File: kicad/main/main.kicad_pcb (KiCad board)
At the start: 2 copper layers, 41 x 41 mm, 11 parts, among them J1 Conn_01x14, J2 Conn_01x14_Socket, J3 Conn_01x04, J4 Conn_01x03_Socket, J5 Conn_01x06, J7 Conn_01x07, J8 Conn_01x09

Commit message: modified:   kicad/main/main.kicad_pcb
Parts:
- added D1: LED, LED_THT:LED_D3.0mm_FlatTop, F.Cu at (135.8, 72.0)
- added R1: R, Resistor_THT:R_Axial_DIN0204_L3.6mm_D1.6mm_P5.08mm_Horizontal, F.Cu at (134.0, 81.2)
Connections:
- J1 pad 11: unconnected-(J1-Pin_11-Pad11) -> /LED
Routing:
- net Net-(D1-A): track 0.00 -> 19.9 mm
- net /GND: track 45.7 -> 61.8 mm
- net /LED: track 0.00 -> 6.01 mm
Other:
- board text added: ">LED"
- board text added: "CS"
- board text added: "LED>"
- board text added: "MISO"
- board text added: "MOSI"
- board text removed: "GND"

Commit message: modified:   kicad/main/main.kicad_pcb
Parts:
- added G***: LOGO, Logo:logo, F.Cu at (145.9, 83.9)

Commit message: modified:   kicad/main/main.kicad_pcb
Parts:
- added J6: Conn_01x08, Connector_PinSocket_2.00mm:PinSocket_1x08_P2.00mm_Vertical, F.Cu at (137.8, 107.5)
- moved R1 1.04 mm to (132.9, 81.2)
- moved G*** 0.69 mm to (145.2, 83.8)
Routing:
- net /MOSI: track 0.00 -> 38.1 mm
- net /MISO: track 0.00 -> 36.3 mm
- net /CS: track 0.00 -> 35.6 mm
- net /SCL1: track 0.00 -> 21.4 mm
- net /SDA1: track 0.00 -> 20.8 mm
- net /SCK: track 0.00 -> 20.4 mm
- net /3V3: track 37.2 -> 42.1 mm
- net /GND: track 61.8 -> 60.1 mm
- net Net-(D1-A): track 19.9 -> 18.8 mm
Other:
- board size 41 x 41 mm -> 41 x 44.5 mm
- board text added: "CL1"
- board text added: "DA1"
- board text added: "SCK"
- board text added: "SI"
- board text added: "SO"

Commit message: modified:   kicad/main/main.kicad_pcb
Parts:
- removed ? (x2): , 
- removed J3: Conn_01x04, Connector_PinHeader_2.00mm:PinHeader_1x04_P2.00mm_Vertical
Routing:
- net /5V: track 24.2 -> 9.60 mm
- net /RX5: track 11.5 -> 0.00 mm
- net /TX5: track 11.2 -> 0.00 mm
- net /GND: track 60.1 -> 57.6 mm

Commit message: modified:   kicad/main/main.kicad_pcb
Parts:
- 220Ω: renamed from R1; footprint Resistor_THT:R_Axial_DIN0204_L3.6mm_D1.6mm_P5.08mm_Horizontal -> Resistor_THT:R_Axial_DIN0204_L3.6mm_D1.6mm_P7.62mm_Horizontal
- moved 220Ω 0.77 mm to (132.8, 80.5), turned to -90 degrees
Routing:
- net /LED: track 5.58 -> 13.5 mm

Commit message: modified:   kicad/main/main.kicad_pcb
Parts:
- added ?: , , F.Cu at (145.2, 104.8)
- added ?: , , F.Cu at (127.8, 86.2)
- moved J6 0.50 mm to (137.8, 108.0)
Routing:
- net /SDA1: track 20.8 -> 21.3 mm
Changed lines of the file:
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@@
 	(footprint "Connector_PinSocket_2.00mm:PinSocket_1x08_P2.00mm_Vertical"
 		(layer "F.Cu")
-		(at 137.75 107.5 90)
+		(at 137.75 108 90)
 		(descr "Through hole straight socket strip, 1x08, 2.00mm pitch, single row (from Kicad 4.0.7), script generated")
 		(tags "Through hole socket strip THT 1x08 2.00mm single row")
@@
 		)
 	)
+	(footprint ""
+		(layer "F.Cu")
+		(at 145.25 104.75)
+		(property "Reference" ""
+			(at 0 0 0)
+			(layer "F.SilkS")
+			(effects
+				(font
+					(size 1.27 1.27)
+					(thickness 0.15)
+				)
+			)
+		)
+		(property "Value" ""
+			(at 0 0 0)
+			(layer "F.Fab")
+			(effects
+				(font
+					(size 1.27 1.27)
+					(thickness 0.15)
+				)
+			)
+		)
+		(property "Datasheet" ""
+			(at 0 0 0)
+			(layer "F.Fab")
+			(hide yes)
+			(effects
+				(font
+					(size 1.27 1.27)
+					(thickness 0.15)
+				)
+			)
+		)
+		(property "Description" ""
+			(at 0 0 0)
+			(layer "F.Fab")
+			(hide yes)
+			(effects
+				(font
+					(size 1.27 1.27)
+					(thickness 0.15)
+				)
+			)
+		)
+		(pad "" np_thru_hole circle
+			(at 0.132999 -0.264 225)
+			(size 2.5 2.5)
+			(drill 2.5)
+			(layers "*.Cu" "*.Mask")
+		)
+		(embedded_fonts no)
+	)
 	(footprint "Connector_PinHeader_2.54mm:PinHeader_1x03_P2.54mm_Vertical"
 		(layer "F.Cu")
@@
 		(embedded_fonts no)
 	)
+	(footprint ""
+		(layer "F.Cu")
+		(at 127.75 86.25)
+		(property "Reference" ""
+			(at 0 0 0)
+			(layer "F.SilkS")
+			(effects
+				(font
+					(size 1.27 1.27)
+					(thickness 0.15)
+				)
+			)
+		)
+		(property "Value" ""
+			(at 0 0 0)
+			(layer "F.Fab")
+			(effects
+				(font
+					(size 1.27 1.27)
+					(thickness 0.15)
+				)
+			)
+		)
+		(property "Datasheet" ""
+			(at 0 0 0)
+			(layer "F.Fab")
+			(hide yes)
+			(effects
+				(font
+					(size 1.27 1.27)
+					(thickness 0.15)
+				)
+			)
+		)
+		(property "Description" ""
+			(at 0 0 0)
+			(layer "F.Fab")
+			(hide yes)
+			(effects
+				(font
+					(size 1.27 1.27)
+					(thickness 0.15)
+				)
+			)
+		)
+		(pad "" np_thru_hole circle
+			(at -0.3983 0.204794 225)
+			(size 2.5 2.5)
+			(drill 2.5)
+			(layers "*.Cu" "*.Mask")
+		)
+		(embedded_fonts no)
+	)
 	(gr_poly
 		(pts
@@
 	)
 	(gr_text "SI"
-		(at 141 109.5 0)
+		(at 141 110 0)
 		(layer "F.SilkS")
 		(effects
@@
 	)
 	(gr_text "SO"
-		(at 139 106.5 0)
+		(at 139 107 0)
 		(layer "F.SilkS")
 		(effects
@@
 	)
 	(gr_text "GD"
-		(at 149 109.5 0)
+		(at 149 110 0)
 		(layer "F.SilkS")
 		(effects
@@
 	)
 	(gr_text "SCK"
-		(at 136.5 109.5 0)
+		(at 136.5 110 0)
 		(layer "F.SilkS")
 		(effects
@@
 	)
 	(gr_text "3V3"
-		(at 150.5 106.5 0)
+		(at 150.5 107 0)
 		(layer "F.SilkS")
 		(effects
@@
 	)
 	(gr_text "CL1"
-		(at 144.5 109.5 0)
+		(at 144.5 110 0)
 		(layer "F.SilkS")
 		(effects
@@
 	)
 	(gr_text "CS"
-		(at 142.75 106.5 0)
+		(at 142.75 107 0)
 		(layer "F.SilkS")
 		(effects
@@
 	)
 	(gr_text "DA1"
-		(at 146.5 106.5 0)
+		(at 146.5 107 0)
 		(layer "F.SilkS")
 		(effects
@@
 	)
 	(gr_text "SI"
-		(at 142.25 109.5 0)
+		(at 142.25 110 0)
 		(layer "B.SilkS")
 		(effects
@@
 	)
 	(gr_text "SO"
-		(at 140.75 106.5 0)
+		(at 140.75 107 0)
 		(layer "B.SilkS")
 		(effects
@@
 	)
 	(gr_text "SCK"
-		(at 139 109.5 0)
+		(at 139 110 0)
 		(layer "B.SilkS")
 		(effects
@@
 	)
 	(gr_text "GD"
-		(at 150.75 109.5 0)
+		(at 150.75 110 0)
 		(layer "B.SilkS")
 		(effects
@@
 	)
 	(gr_text "CS"
-		(at 144.5 106.5 0)
+		(at 144.5 107 0)
 		(layer "B.SilkS")
 		(effects
@@
 	)
 	(gr_text "CL1"
-		(at 146.75 109.5 0)
+		(at 146.75 110 0)
 		(layer "B.SilkS")
 		(effects
@@
 	)
 	(gr_text "3V3"
-		(at 152.75 106.5 0)
+		(at 152.75 107 0)
 		(layer "B.SilkS")
 		(effects
@@
 	)
 	(gr_text "DA1"
-		(at 148.75 106.5 0)
+		(at 148.75 107 0)
 		(layer "B.SilkS")
 		(effects
@@
 	)
 	(segment
-		(start 142.25 106)
-		(end 143.75 107.5)
-		(width 0.2)
-		(layer "B.Cu")
-		(net 1)
-	)
-	(segment
-		(start 139.75 96.02776)
-		(end 139.75 104)
-		(width 0.2)
-		(layer "B.Cu")
-		(net 1)
-	)
-	(segment
 		(start 135.449 77.639)
 		(end 135.449 91.72676)
@@
 	)
 	(segment
-		(start 141.75 106)
-		(end 142.25 106)
+		(start 134.06 76.25)
+		(end 135.449 77.639)
 		(width 0.2)
 		(layer "B.Cu")
@@
 	)
 	(segment
-		(start 139.75 104)
-		(end 141.75 106)
+		(start 139.75 96.02776)
+		(end 139.75 104)
 		(width 0.2)
 		(layer "B.Cu")
@@
 	)
 	(segment
-		(start 134.06 76.25)
-		(end 135.449 77.639)
+		(start 139.75 104)
+		(end 143.75 108)
 		(width 0.2)
 		(layer "B.Cu")
@@
 	)
 	(segment
-		(start 128.98 76.25)
-		(end 130.369 77.639)
+		(start 138.274 106.524)
+		(end 139.75 108)
 		(width 0.2)
 		(layer "B.Cu")
@@
 	)
 	(segment
-		(start 137.774 106.524)
-		(end 138.774 106.524)
+		(start 128.98 76.25)
+		(end 130.369 77.639)
 		(width 0.2)
 		(layer "B.Cu")
@@
 	)
 	(segment
-		(start 130.369 77.639)
-		(end 130.369 99.119)
+		(start 137.774 106.524)
+		(end 138.274 106.524)
 		(width 0.2)
 		(layer "B.Cu")
@@
 	)
 	(segment
-		(start 138.774 106.524)
-		(end 139.75 107.5)
+		(start 130.369 77.639)
+		(end 130.369 99.119)
 		(width 0.2)
 		(layer "B.Cu")
@@
 	(segment
 		(start 141.90855 105.59145)
-		(end 142.84145 105.59145)
-		(width 0.2)
-		(layer "B.Cu")
-		(net 12)
-	)
-	(segment
-		(start 143.75 106.5)
-		(end 144.75 106.5)
+		(end 142.721723 105.59145)
 		(width 0.2)
 		(layer "B.Cu")
@@
 	)
 	(segment
-		(start 144.75 106.5)
-		(end 145.75 107.5)
-		(width 0.2)
-		(layer "B.Cu")
-		(net 12)
-	)
-	(segment
-		(start 140.5 104.1829)
-		(end 141.90855 105.59145)
+		(start 142.721723 105.59145)
+		(end 145.130273 108)
 		(width 0.2)
 		(layer "B.Cu")
@@
 	)
 	(segment
-		(start 142.84145 105.59145)
-		(end 143.75 106.5)
+		(start 145.130273 108)
+		(end 145.75 108)
 		(width 0.2)
 		(layer "B.Cu")
@@
 	)
 	(segment
-		(start 145.565743 107.5)
-		(end 145.75 107.5)
+		(start 140.5 104.1829)
+		(end 141.90855 105.59145)
 		(width 0.2)
 		(layer "B.Cu")
@@
 	)
 	(segment
-		(start 139.14 91.25)
-		(end 140.901 93.011)
+		(start 144.25 106.25)
+		(end 146 106.25)
 		(width 0.2)
 		(layer "B.Cu")
@@
 	)
 	(segment
-		(start 140.901 102.268157)
-		(end 144.719843 106.087)
+		(start 146 106.25)
+		(end 147.75 108)
 		(width 0.2)
 		(layer "B.Cu")
@@
 	)
 	(segment
-		(start 146.337 106.087)
-		(end 147.75 107.5)
+		(start 140.901 102.901)
+		(end 144.25 106.25)
 		(width 0.2)
 		(layer "B.Cu")
@@
 	)
 	(segment
-		(start 144.719843 106.087)
-		(end 146.337 106.087)
+		(start 139.14 91.25)
+		(end 140.901 93.011)
 		(width 0.2)
 		(layer "B.Cu")
@@
 	(segment
 		(start 140.901 93.011)
-		(end 140.901 102.268157)
+		(end 140.901 102.901)
 		(width 0.2)
 		(layer "B.Cu")

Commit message: modified:   kicad/main/main.kicad_pcb
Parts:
- renumbered 220Ω to R1
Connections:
- J2 pad 6: /RX5 -> unconnected-(J2-Pin_6-Pad6)
- J2 pad 7: /TX5 -> unconnected-(J2-Pin_7-Pad7)
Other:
- board text removed: "RX5"
- board text removed: "TX5"
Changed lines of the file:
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@@
 	(net 22 "unconnected-(J1-Pin_2-Pad2)")
 	(net 23 "unconnected-(J1-Pin_3-Pad3)")
-	(net 24 "/TX5")
-	(net 25 "/RX5")
+	(net 24 "unconnected-(J2-Pin_7-Pad7)")
+	(net 25 "unconnected-(J2-Pin_6-Pad6)")
 	(net 26 "unconnected-(J2-Pin_12-Pad12)")
 	(net 27 "unconnected-(J2-Pin_13-Pad13)")
@@
 			(layers "*.Cu" "*.Mask")
 			(remove_unused_layers no)
-			(net 25 "/RX5")
+			(net 25 "unconnected-(J2-Pin_6-Pad6)")
 			(pinfunction "Pin_6")
 			(pintype "passive")
@@
 			(layers "*.Cu" "*.Mask")
 			(remove_unused_layers no)
-			(net 24 "/TX5")
+			(net 24 "unconnected-(J2-Pin_7-Pad7)")
 			(pinfunction "Pin_7")
 			(pintype "passive")
@@
 		(descr "Resistor, Axial_DIN0204 series, Axial, Horizontal, pin pitch=7.62mm, 0.167W, length*diameter=3.6*1.6mm^2, http://cdn-reichelt.de/documents/datenblatt/B400/1_4W%23YAG.pdf")
 		(tags "Resistor Axial_DIN0204 series Axial Horizontal pin pitch 7.62mm 0.167W length 3.6mm diameter 1.6mm")
-		(property "Reference" "220Ω"
+		(property "Reference" "R1"
 			(at 3.81 0 90)
 			(layer "F.SilkS")
@@
 		)
 	)
-	(gr_text "RX5"
-		(at 149.8 95 90)
-		(layer "F.SilkS")
-		(effects
-			(font
-				(size 0.8 0.8)
-				(thickness 0.15)
-			)
-			(justify left bottom)
-		)
-	)
 	(gr_text "GD"
 		(at 161.231223 74.98 0)
@@
 		(layer "F.SilkS")
 		(effects
-			(font
-				(size 0.8 0.8)
-				(thickness 0.15)
-			)
-			(justify left bottom)
-		)
-	)
-	(gr_text "TX5"
-		(at 147.15 94.85 90)
-		(layer "F.SilkS")
-		(effects

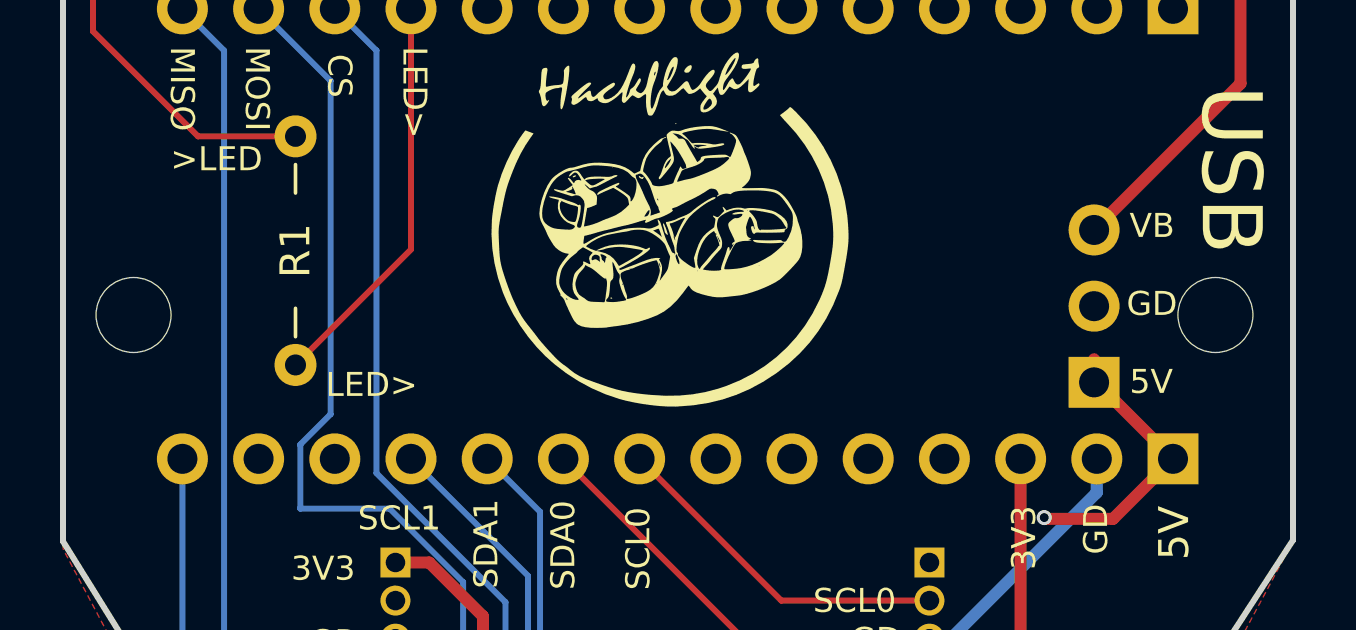
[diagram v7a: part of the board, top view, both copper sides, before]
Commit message: Schematic has separate component for each hole
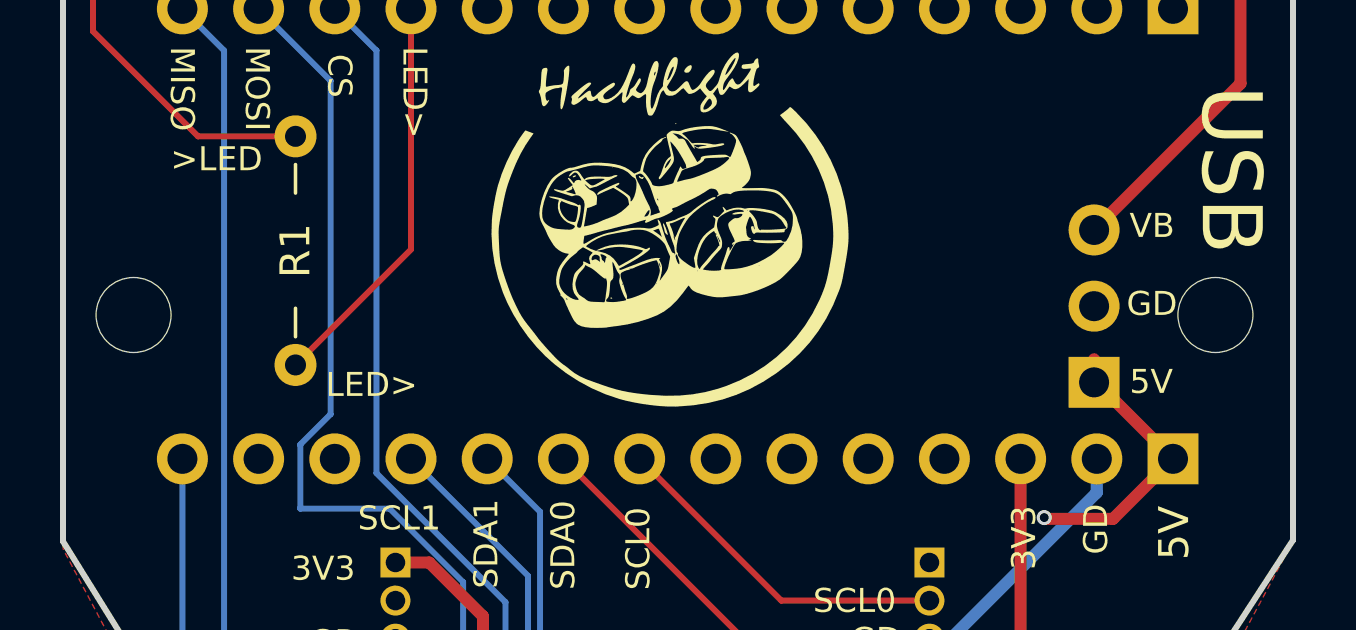
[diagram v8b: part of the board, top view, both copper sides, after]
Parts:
- removed ? (x2): , 
- removed the H1 at (163.1, 88.6)
- added H2: MountingHole, MountingHole:MountingHole_2.5mm, F.Cu at (166.2, 86.5)
- added H3: MountingHole, MountingHole:MountingHole_2.5mm, F.Cu at (173.2, 90.2)
- added H4: MountingHole, MountingHole:MountingHole_2.5mm, F.Cu at (127.4, 86.5)
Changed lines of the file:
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@@
 	(net 38 "Net-(D1-A)")
 	(net 39 "/LED")
+	(footprint "MountingHole:MountingHole_2.5mm"
+		(layer "F.Cu")
+		(at 173.25 90.2)
+		(descr "Mounting Hole 2.5mm, no annular, generated by kicad-footprint-generator mountinghole.py")
+		(tags "mountinghole")
+		(property "Reference" "H3"
+			(at 0 -3.45 0)
+			(layer "F.SilkS")
+			(hide yes)
+			(effects
+				(font
+					(size 1 1)
+					(thickness 0.15)
+				)
+			)
+		)
+		(property "Value" "MountingHole"
+			(at 0 3.45 0)
+			(layer "F.Fab")
+			(hide yes)
+			(effects
+				(font
+					(size 1 1)
+					(thickness 0.15)
+				)
+			)
+		)
+		(property "Datasheet" "~"
+			(at 0 0 0)
+			(layer "F.Fab")
+			(hide yes)
+			(effects
+				(font
+					(size 1.27 1.27)
+					(thickness 0.15)
+				)
+			)
+		)
+		(property "Description" "Mounting Hole without connection"
+			(at 0 0 0)
+			(layer "F.Fab")
+			(hide yes)
+			(effects
+				(font
+					(size 1.27 1.27)
+					(thickness 0.15)
+				)
+			)
+		)
+		(property ki_fp_filters "MountingHole*")
+		(sheetname "/")
+		(sheetfile "main.kicad_sch")
+		(attr exclude_from_pos_files exclude_from_bom)
+		(pad "" np_thru_hole circle
+			(at -27.867 14.286)
+			(size 2.5 2.5)
+			(drill 2.5)
+			(layers "*.Cu" "*.Mask")
+		)
+		(embedded_fonts no)
+	)
+	(footprint "MountingHole:MountingHole_2.5mm"
+		(layer "F.Cu")
+		(at 127.352 86.455)
+		(descr "Mounting Hole 2.5mm, no annular, generated by kicad-footprint-generator mountinghole.py")
+		(tags "mountinghole")
+		(property "Reference" "H4"
+			(at 0 -3.45 0)
+			(layer "F.SilkS")
+			(hide yes)
+			(effects
+				(font
+					(size 1 1)
+					(thickness 0.15)
+				)
+			)
+		)
+		(property "Value" "MountingHole"
+			(at 0 3.45 0)
+			(layer "F.Fab")
+			(hide yes)
+			(effects
+				(font
+					(size 1 1)
+					(thickness 0.15)
+				)
+			)
+		)
+		(property "Datasheet" "~"
+			(at 0 0 0)
+			(layer "F.Fab")
+			(hide yes)
+			(effects
+				(font
+					(size 1.27 1.27)
+					(thickness 0.15)
+				)
+			)
+		)
+		(property "Description" "Mounting Hole without connection"
+			(at 0 0 0)
+			(layer "F.Fab")
+			(hide yes)
+			(effects
+				(font
+					(size 1.27 1.27)
+					(thickness 0.15)
+				)
+			)
+		)
+		(property ki_fp_filters "MountingHole*")
+		(sheetname "/")
+		(sheetfile "main.kicad_sch")
+		(attr exclude_from_pos_files exclude_from_bom)
+		(pad "" np_thru_hole circle
+			(at 0 0)
+			(size 2.5 2.5)
+			(drill 2.5)
+			(layers "*.Cu" "*.Mask")
+		)
+		(embedded_fonts no)
+	)
+	(footprint "MountingHole:MountingHole_2.5mm"
+		(layer "F.Cu")
+		(at 166.25 86.5)
+		(descr "Mounting Hole 2.5mm, no annular, generated by kicad-footprint-generator mountinghole.py")
+		(tags "mountinghole")
+		(property "Reference" "H2"
+			(at 0 -3.45 0)
+			(layer "F.SilkS")
+			(hide yes)
+			(effects
+				(font
+					(size 1 1)
+					(thickness 0.15)
+				)
+			)
+		)
+		(property "Value" "MountingHole"
+			(at 0 3.45 0)
+			(layer "F.Fab")
+			(hide yes)
+			(effects
+				(font
+					(size 1 1)
+					(thickness 0.15)
+				)
+			)
+		)
+		(property "Datasheet" "~"
+			(at 0 0 0)
+			(layer "F.Fab")
+			(hide yes)
+			(effects
+				(font
+					(size 1.27 1.27)
+					(thickness 0.15)
+				)
+			)
+		)
+		(property "Description" "Mounting Hole without connection"
+			(at 0 0 0)
+			(layer "F.Fab")
+			(hide yes)
+			(effects
+				(font
+					(size 1.27 1.27)
+					(thickness 0.15)
+				)
+			)
+		)
+		(property ki_fp_filters "MountingHole*")
+		(sheetname "/")
+		(sheetfile "main.kicad_sch")
+		(attr exclude_from_pos_files exclude_from_bom)
+		(pad "" np_thru_hole circle
+			(at -2.836 -0.045)
+			(size 2.5 2.5)
+			(drill 2.5)
+			(layers "*.Cu" "*.Mask")
+		)
+		(embedded_fonts no)
+	)
 	(footprint "Connector_PinHeader_1.27mm:PinHeader_1x09_P1.27mm_Vertical"
 		(layer "F.Cu")
@@
 		(embedded_fonts no)
 	)
-	(footprint "MountingHole:MountingHole_2.5mm"
-		(layer "F.Cu")
-		(at 163.101704 88.625281 -135)
-		(descr "Mounting Hole 2.5mm, no annular, generated by kicad-footprint-generator mountinghole.py")
-		(tags "mountinghole")
-		(property "Reference" "H1"
-			(at 0 -3.449999 45)
-			(layer "F.SilkS")
-			(hide yes)
-			(effects
-				(font
-					(size 1 1)
-					(thickness 0.15)
-				)
-			)
-		)
-		(property "Value" "MountingHole"
-			(at 0 3.449999 45)
-			(layer "F.Fab")
-			(hide yes)
-			(effects
-				(font
-					(size 1 1)
-					(thickness 0.15)
-				)
-			)
-		)
-		(property "Datasheet" "~"
-			(at 0 0 45)
-			(layer "F.Fab")
-			(hide yes)
-			(effects
-				(font
-					(size 1.27 1.27)
-					(thickness 0.15)
-				)
-			)
-		)
-		(property "Description" "Mounting Hole without connection"
-			(at 0 0 45)
-			(layer "F.Fab")
-			(hide yes)
-			(effects
-				(font
-					(size 1.27 1.27)
-					(thickness 0.15)
-				)
-			)
-		)
-		(property ki_fp_filters "MountingHole*")
-		(sheetname "/")
-		(sheetfile "main.kicad_sch")
-		(attr exclude_from_pos_files exclude_from_bom)
-		(pad "" np_thru_hole circle
-			(at -1.75575 1.313782 225)
-			(size 2.5 2.5)
-			(drill 2.5)
-			(layers "*.Cu" "*.Mask")
-		)
-		(embedded_fonts no)
-	)
 	(footprint "Connector_PinSocket_2.00mm:PinSocket_1x06_P2.00mm_Vertical"
 		(layer "F.Cu")
@@
 		)
 	)
-	(footprint ""
-		(layer "F.Cu")
-		(at 145.25 104.75)
-		(property "Reference" ""
-			(at 0 0 0)
-			(layer "F.SilkS")
-			(effects
-				(font
-					(size 1.27 1.27)
-					(thickness 0.15)
-				)
-			)
-		)
-		(property "Value" ""
-			(at 0 0 0)
-			(layer "F.Fab")
-			(effects
-				(font
-					(size 1.27 1.27)
-					(thickness 0.15)
-				)
-			)
-		)
-		(property "Datasheet" ""
-			(at 0 0 0)
-			(layer "F.Fab")
-			(hide yes)
-			(effects
-				(font
-					(size 1.27 1.27)
-					(thickness 0.15)
-				)
-			)
-		)
-		(property "Description" ""
-			(at 0 0 0)
-			(layer "F.Fab")
-			(hide yes)
-			(effects
-				(font
-					(size 1.27 1.27)
-					(thickness 0.15)
-				)
-			)
-		)
-		(pad "" np_thru_hole circle
-			(at 0.132999 -0.264 225)
-			(size 2.5 2.5)
-			(drill 2.5)
-			(layers "*.Cu" "*.Mask")
-		)
-		(embedded_fonts no)
-	)
 	(footprint "Connector_PinHeader_2.54mm:PinHeader_1x03_P2.54mm_Vertical"
 		(layer "F.Cu")
@@
 			(size 2.5 2.5)
 			(drill 2.5)
-			(layers "*.Cu" "*.Mask")
-		)
-		(embedded_fonts no)
-	)
-	(footprint ""
-		(layer "F.Cu")
-		(at 127.75 86.25)
-		(property "Reference" ""
-			(at 0 0 0)
-			(layer "F.SilkS")
-			(effects
-				(font
-					(size 1.27 1.27)
-					(thickness 0.15)
-				)
-			)
-		)
-		(property "Value" ""
-			(at 0 0 0)
-			(layer "F.Fab")
-			(effects
-				(font
-					(size 1.27 1.27)
-					(thickness 0.15)
-				)
-			)
-		)
-		(property "Datasheet" ""
-			(at 0 0 0)
-			(layer "F.Fab")
-			(hide yes)
-			(effects
-				(font
-					(size 1.27 1.27)
-					(thickness 0.15)
-				)
-			)
-		)
-		(property "Description" ""
-			(at 0 0 0)
-			(layer "F.Fab")
-			(hide yes)
-			(effects
-				(font
-					(size 1.27 1.27)
-					(thickness 0.15)
-				)
-			)
-		)
-		(pad "" np_thru_hole circle
-			(at -0.3983 0.204794 225)
-			(size 2.5 2.5)
-			(drill 2.5)
